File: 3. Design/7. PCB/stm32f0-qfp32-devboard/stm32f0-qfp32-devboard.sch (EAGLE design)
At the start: 12 parts, among them IC1 STM32F051

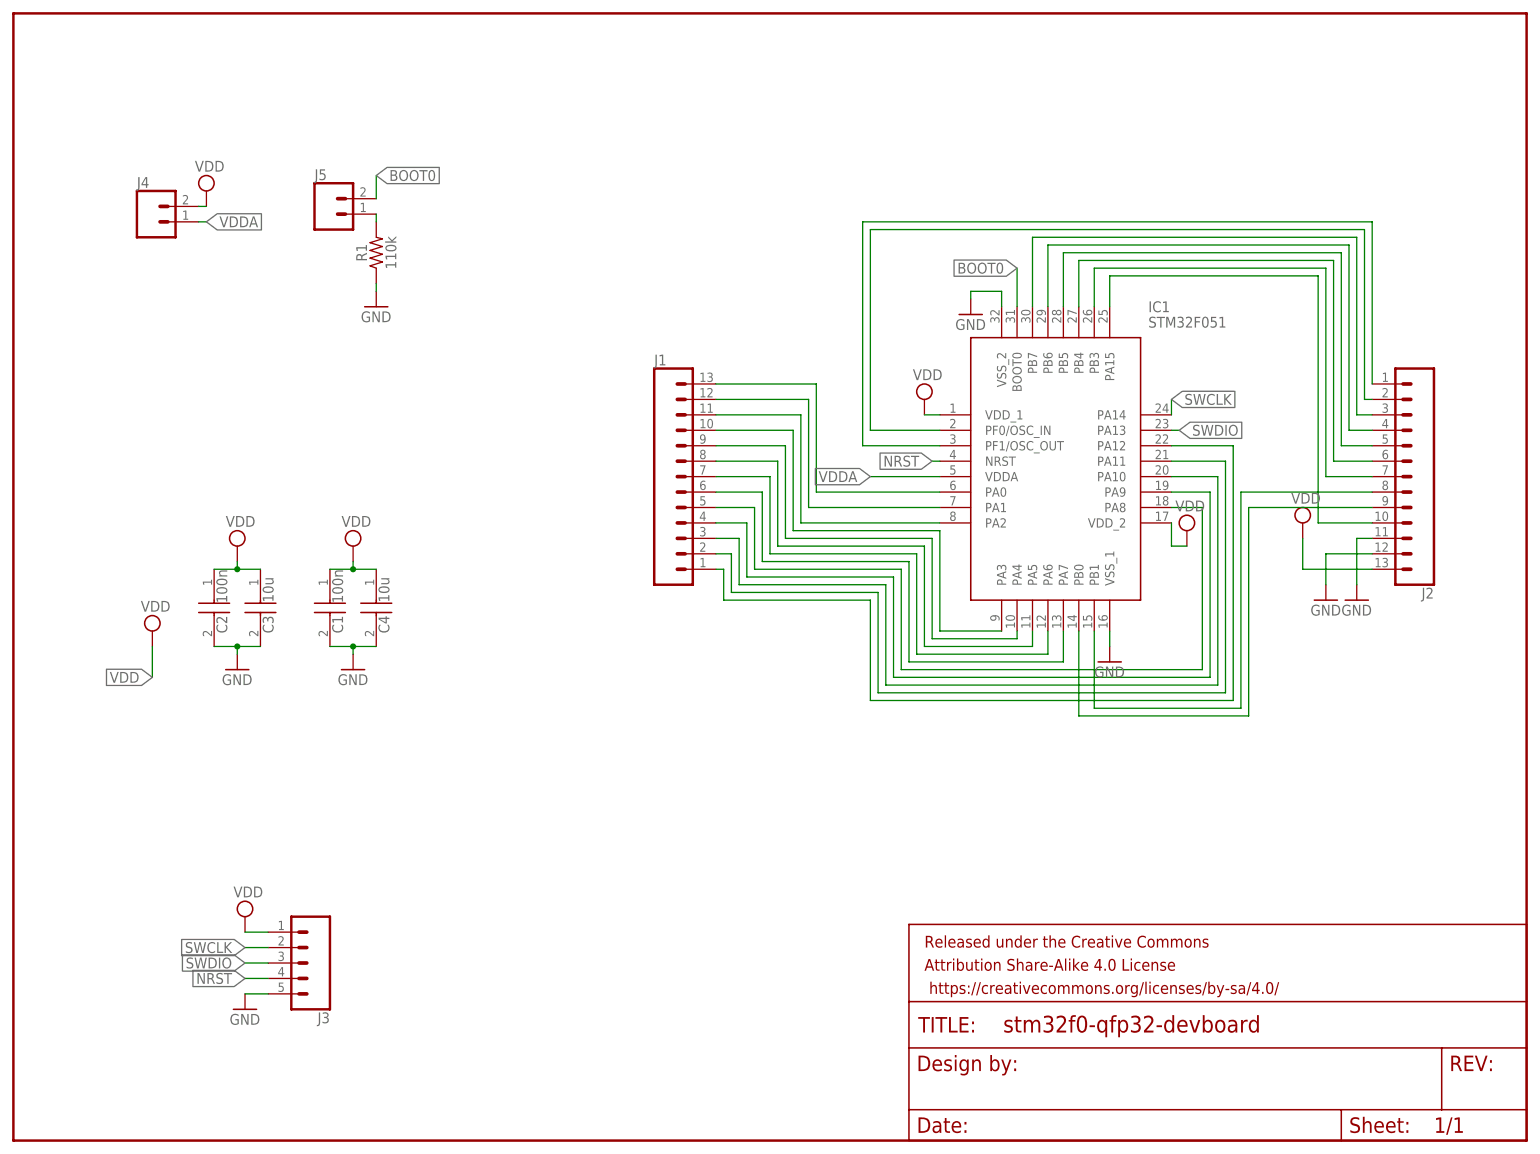
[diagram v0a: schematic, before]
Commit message: ADD|UPDT|FIX: Corrected Dev Board exports and finished wristband board's schematic
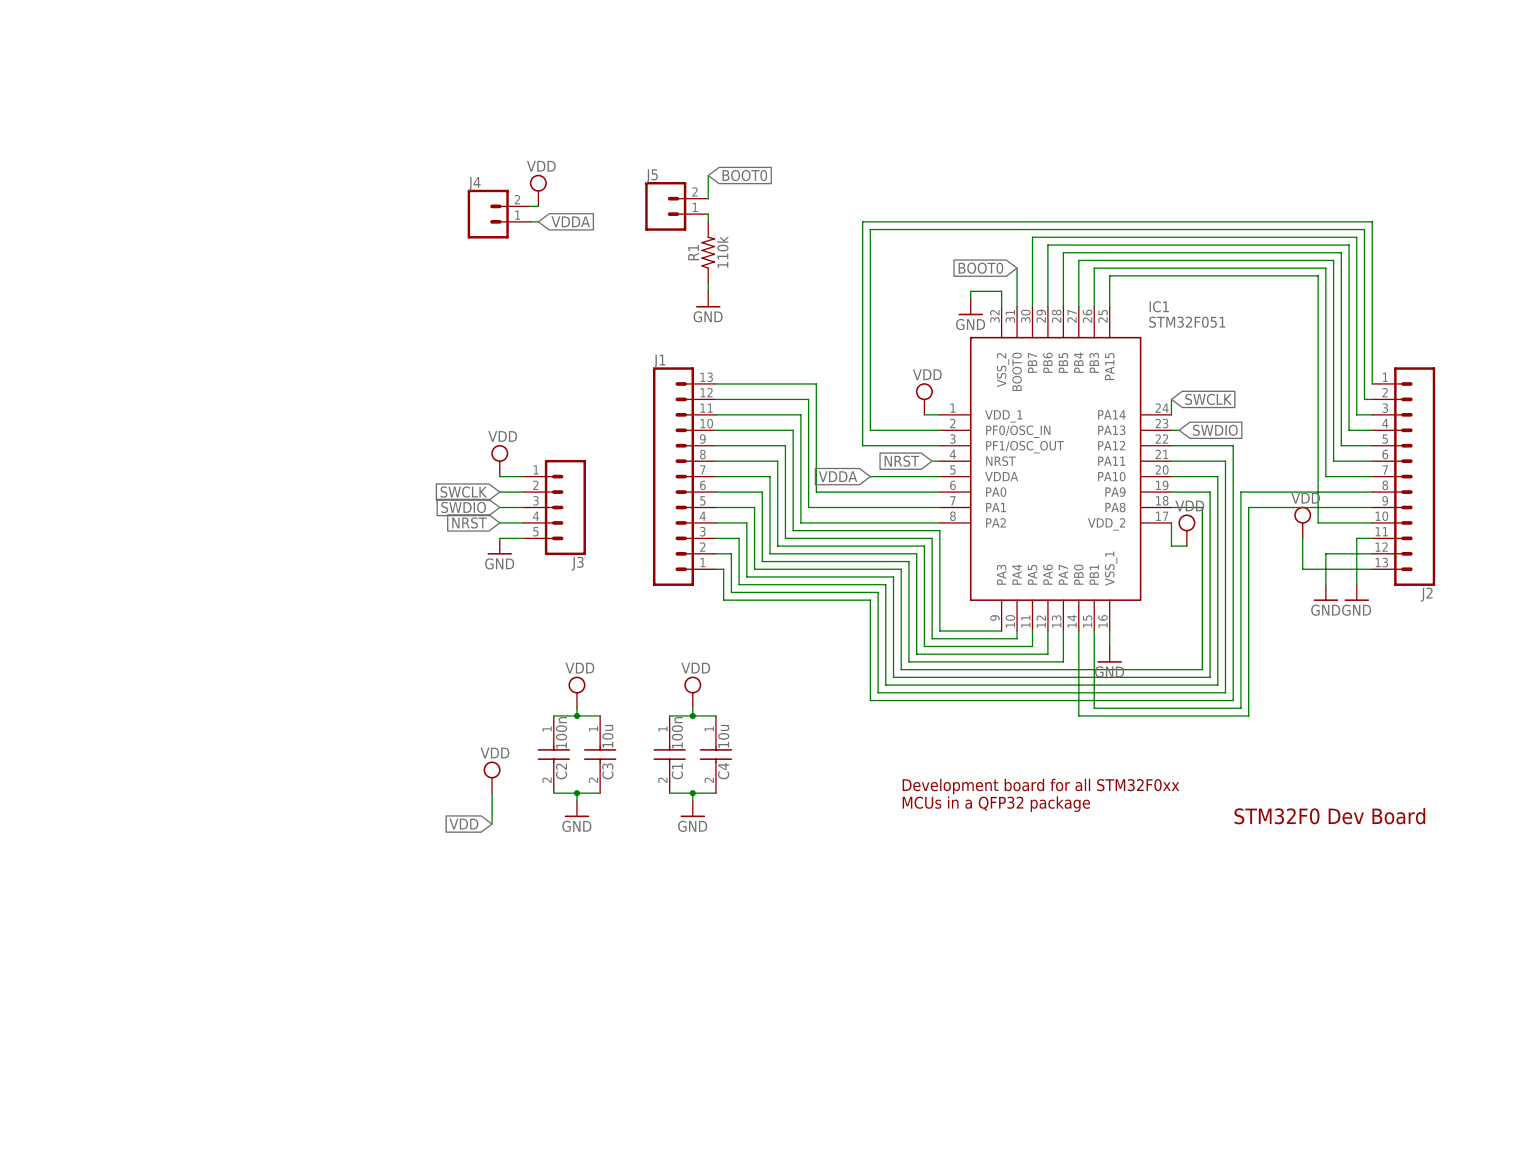
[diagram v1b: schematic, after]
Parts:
- removed FRAME2: FRAME-LETTERNO_PACKAGE, SparkFun-Aesthetics:FRAME-LETTERNO_PACKAGE
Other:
- note added: "Development board for all STM32F0xx MCUs in a QFP32 package"
- note added: "STM32F0 Dev Board"
- moved on the sheet: C1, C2, C3, C4, J3, J4, J5, R1
